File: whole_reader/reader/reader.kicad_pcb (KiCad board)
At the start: 2 copper layers, 50 x 58.5 mm, 61 parts, among them U1 LM386, U2 STM32F103C8T6, U3 MCP16301Hx-xCH, U4 MAX3232, Y1 16MHz

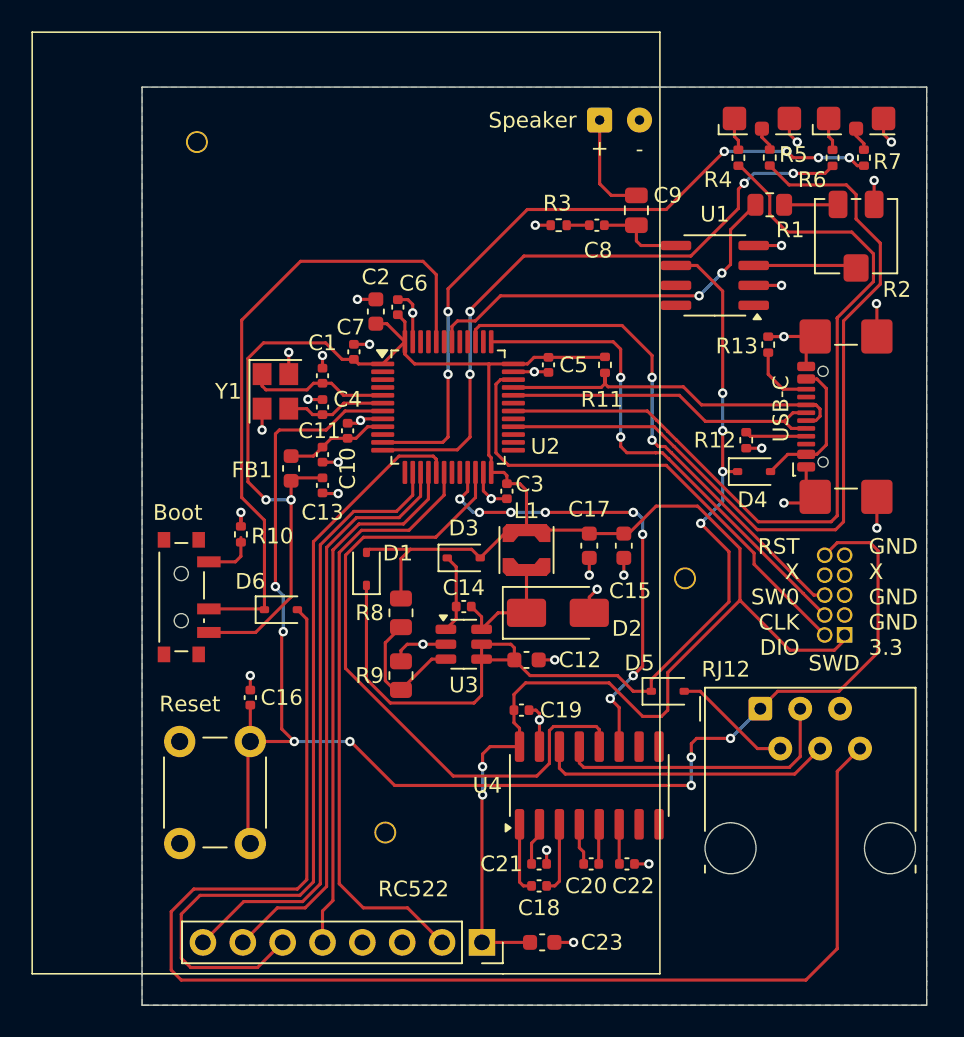
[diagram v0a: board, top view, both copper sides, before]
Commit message: Added toplayer ground copper pour
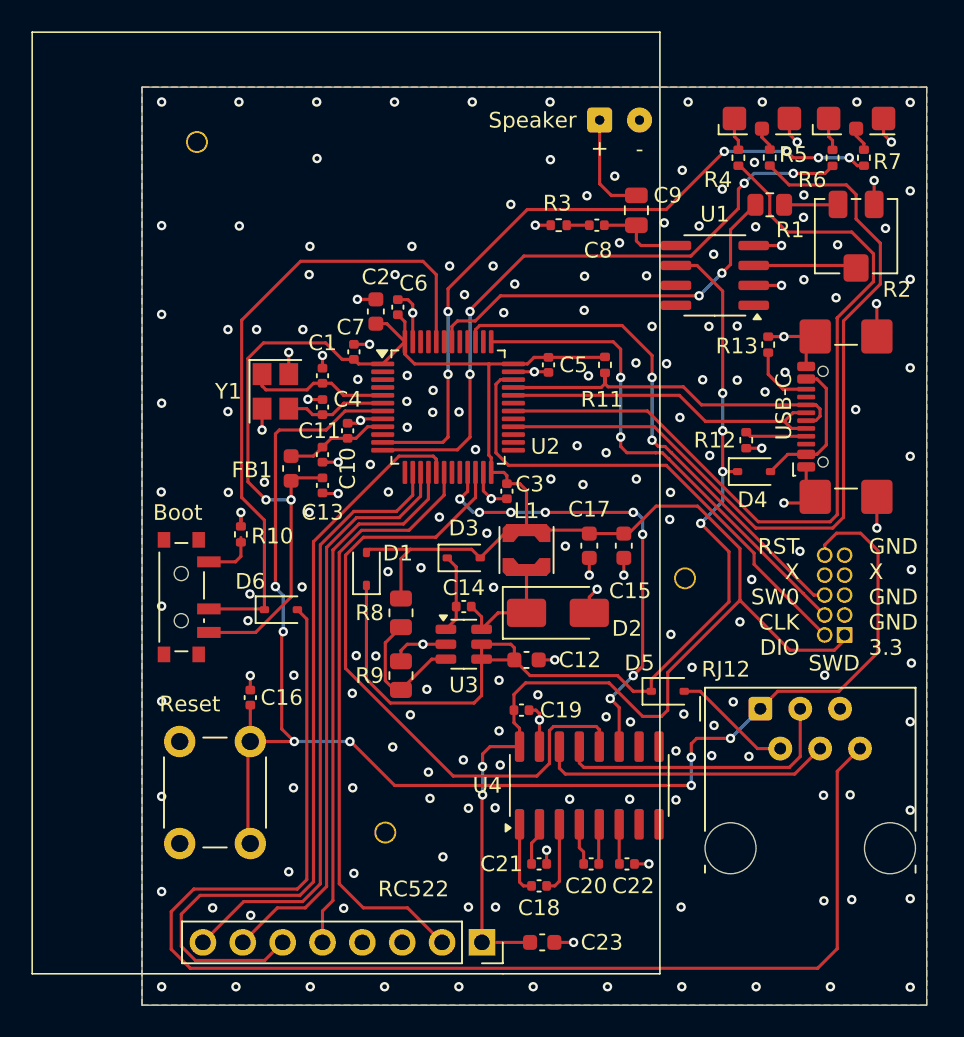
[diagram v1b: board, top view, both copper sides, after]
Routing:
- net Net-(D6-A): track 87.5 -> 86.1 mm
- net NRST: track 93.4 -> 94.3 mm
- net RFID_MOSI: track 52.1 -> 51.3 mm
- net GND: vias 34 -> 198
- added copper zone on F.Cu, net GND

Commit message: RST -> NRST, BOOT -> BOOT0, popis pre SWD
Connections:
- net BOOT renamed BOOT0
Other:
- board text added: "GND X GND GND 3.3V"
- board text added: "NRST X TRSW0 SWCLK SWDIO"
- board text removed: "GND X GND GND 3.3"
- board text removed: "RST X SW0 CLK DIO"
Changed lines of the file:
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@@
 	(net 19 "Net-(D5-A)")
 	(net 20 "Net-(D6-A)")
-	(net 21 "BOOT")
+	(net 21 "BOOT0")
 	(net 22 "SWCLK")
 	(net 23 "SWDIO")
@@
 			(size 0.7 1.5)
 			(layers "F.Cu" "F.Mask" "F.Paste")
-			(net 21 "BOOT")
+			(net 21 "BOOT0")
 			(pinfunction "B")
 			(pintype "passive")
@@
 			(layers "F.Cu" "F.Mask" "F.Paste")
 			(roundrect_rratio 0.25)
-			(net 21 "BOOT")
+			(net 21 "BOOT0")
 			(pinfunction "K")
 			(pintype "passive")
@@
 			(layers "F.Cu" "F.Mask" "F.Paste")
 			(roundrect_rratio 0.25)
-			(net 21 "BOOT")
+			(net 21 "BOOT0")
 			(pinfunction "BOOT0")
 			(pintype "input")
@@
 	(footprint "Connector_PinSocket_1.27mm:PinSocket_2x05_P1.27mm_Vertical"
 		(layer "B.Cu")
-		(at 177.27 62.41)
+		(at 177.2575 62.41)
 		(descr "Through hole straight socket strip, 2x05, 1.27mm pitch, double cols (from Kicad 4.0.7), script generated")
 		(tags "Through hole socket strip THT 2x05 1.27mm double row")
@@
 		)
 	)
-	(gr_text "RST\nX\nSW0\nCLK\nDIO"
-		(at 174.4 63.8 0)
+	(gr_text "NRST\nX\nTRSW0\nSWCLK\nSWDIO"
+		(at 174.625 63.675513 0)
 		(layer "F.SilkS")
 		(effects
@@
 		)
 	)
-	(gr_text "GND\nX\nGND\nGND\n3.3"
-		(at 178.8 63.8 0)
+	(gr_text "GND\nX\nGND\nGND\n3.3V"
+		(at 178.6 63.675513 0)
 		(layer "F.SilkS")
 		(effects
@@
 	)
 	(gr_text "SWD"
-		(at 176.6 64.8 0)
+		(at 176.6125 64.8 0)
 		(layer "F.SilkS")
 		(effects
@@
 	)
 	(via
-		(at 170.6 61.575)
+		(at 170.6 61.125)
 		(size 0.6)
 		(drill 0.3)

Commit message: Oprava pre PWR_FLAG, doplnenie dátumu a revízie
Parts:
- C16, C8: value 100nF -> 100 nF
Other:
- board text added: "UACS reader Rev. 1.0 (2025/04)"
- board text removed: "UACS reader HW ver. 1.0 (2025/04)"

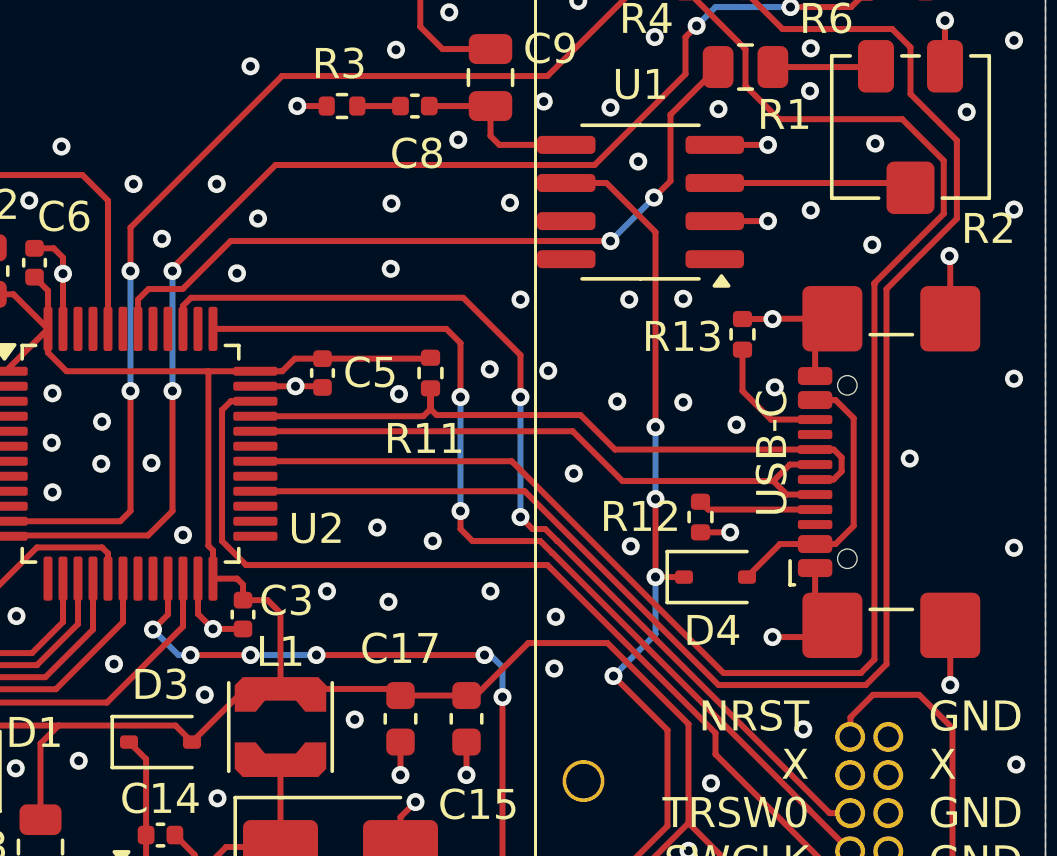
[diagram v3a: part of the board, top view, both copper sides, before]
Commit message: viring diferential pair
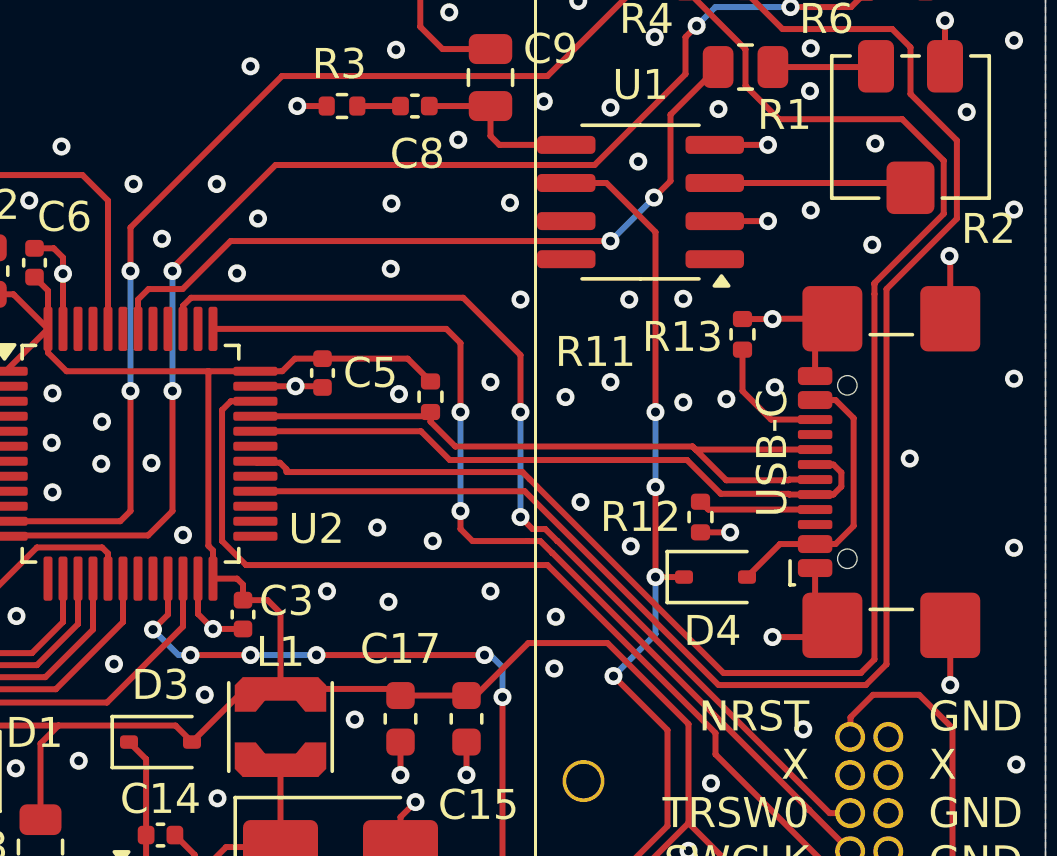
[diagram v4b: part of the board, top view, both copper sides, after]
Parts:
- moved R11 0.79 mm to (162.0, 46.0)
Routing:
- net USB_D+: track 22.9 -> 24.0 mm
- net USB_D-: track 21.2 -> 22.0 mm

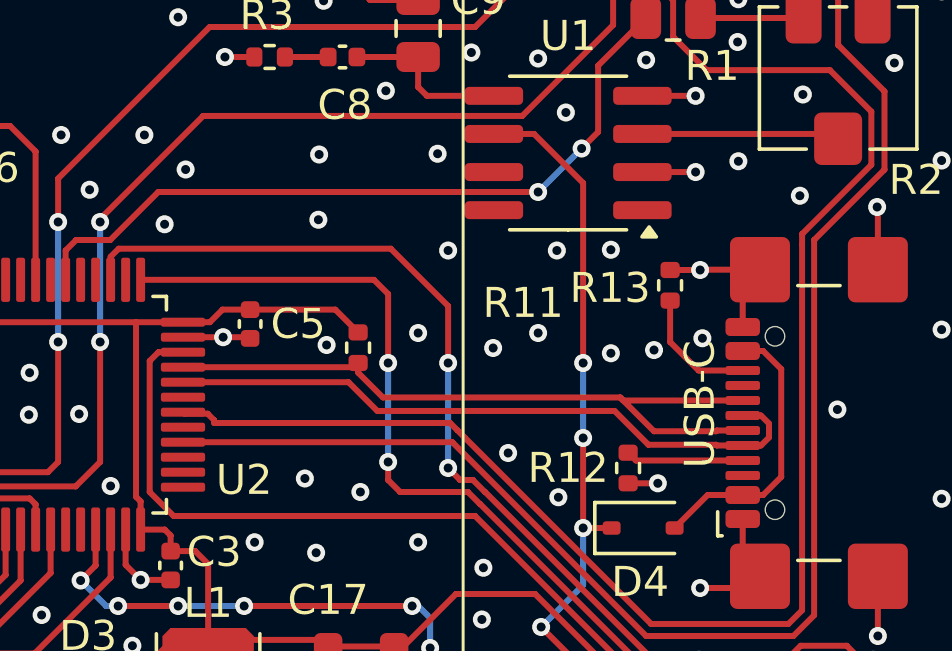
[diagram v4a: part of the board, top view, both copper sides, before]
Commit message: wired diferential pair on usb
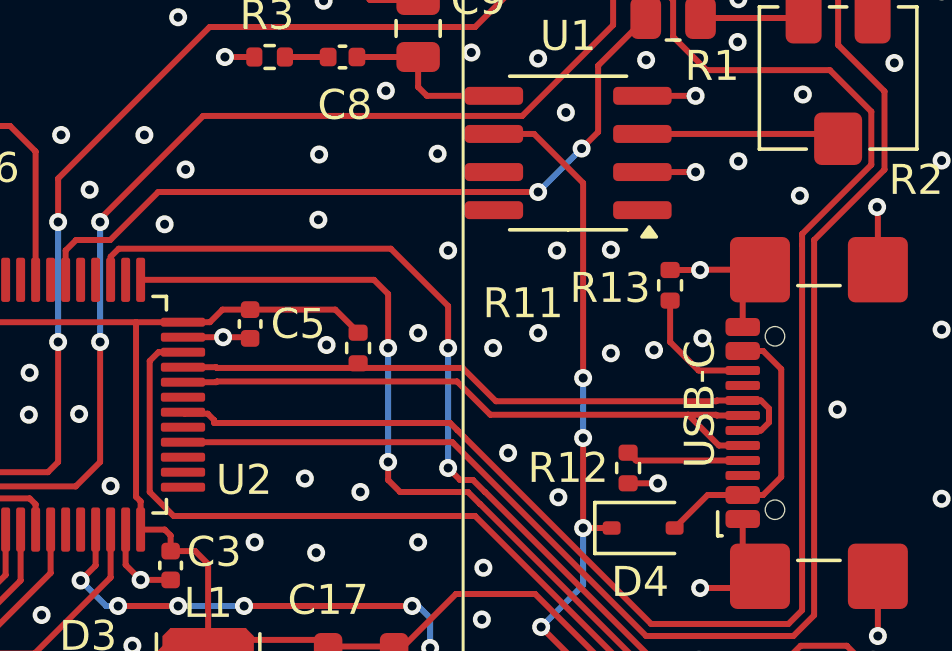
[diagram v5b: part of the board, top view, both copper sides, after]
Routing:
- net USB_D+: track 24.0 -> 21.6 mm
- net USB_D-: track 22.0 -> 21.4 mm
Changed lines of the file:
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@@
 	(footprint "Resistor_SMD:R_0402_1005Metric"
 		(layer "F.Cu")
-		(at 162 45.99 -90)
+		(at 162 46 -90)
 		(descr "Resistor SMD 0402 (1005 Metric), square (rectangular) end terminal, IPC_7351 nominal, (Body size source: IPC-SM-782 page 72, https://www.pcb-3d.com/wordpress/wp-content/uploads/ipc-sm-782a_amendment_1_and_2.pdf), generated with kicad-footprint-generator")
 		(tags "resistor")
@@
 	)
 	(segment
-		(start 169.5 46.5)
+		(start 169.5 47)
 		(end 169.5 40.5)
 		(width 0.2)
@@
 	)
 	(segment
+		(start 169.5 52)
+		(end 169.5 49)
+		(width 0.2)
+		(layer "F.Cu")
+		(net 8)
+	)
+	(segment
+		(start 167.865 38.865)
+		(end 166.525 38.865)
+		(width 0.2)
+		(layer "F.Cu")
+		(net 8)
+	)
+	(segment
 		(start 168.227094 55.172906)
 		(end 168.227094 55.427094)
@@
 	)
 	(segment
-		(start 167.865 38.865)
-		(end 166.525 38.865)
-		(width 0.2)
-		(layer "F.Cu")
-		(net 8)
-	)
-	(segment
 		(start 169.9 57.1)
 		(end 169.9 60.3)
@@
 	)
 	(segment
-		(start 156 63)
-		(end 154.138 63)
+		(start 169.5 40.5)
+		(end 167.865 38.865)
 		(width 0.2)
 		(layer "F.Cu")
@@
 	)
 	(segment
-		(start 169.5 52)
-		(end 169.5 49)
+		(start 156 63)
+		(end 154.138 63)
 		(width 0.2)
 		(layer "F.Cu")
@@
 	)
 	(segment
-		(start 169.5 40.5)
-		(end 167.865 38.865)
-		(width 0.2)
-		(layer "F.Cu")
-		(net 8)
-	)
-	(segment
 		(start 153.6546 66.7454)
 		(end 148.324 66.7454)
@@
 	)
 	(via
-		(at 169.5 46.5)
+		(at 169.5 47)
 		(size 0.6)
 		(drill 0.3)
@@
 	)
 	(segment
-		(start 169.5 52)
-		(end 169.5 53.9)
+		(start 169.5 49)
+		(end 169.5 47)
 		(width 0.2)
 		(layer "B.Cu")
@@
 	)
 	(segment
-		(start 169.5 49)
-		(end 169.5 46.5)
+		(start 169.5 52)
+		(end 169.5 53.9)
 		(width 0.2)
 		(layer "B.Cu")
@@
 	)
 	(segment
+		(start 163 46)
+		(end 163 44.2)
+		(width 0.2)
+		(layer "F.Cu")
+		(net 22)
+	)
+	(segment
 		(start 165.2329 50.8)
 		(end 165.2339 50.801)
@@
 	)
 	(segment
-		(start 163 46.5)
-		(end 163 44.2)
-		(width 0.2)
-		(layer "F.Cu")
-		(net 22)
-	)
-	(segment
 		(start 163 44.2)
 		(end 162.5275 43.7275)
@@
 	)
 	(via
-		(at 163 46.5)
+		(at 163 46)
 		(size 0.6)
 		(drill 0.3)
@@
 	)
 	(segment
-		(start 163 46.5)
+		(start 163 46)
 		(end 163 49.8)
 		(width 0.2)
@@
 	)
 	(segment
-		(start 165 46.5)
+		(start 165 46)
 		(end 165 44.6)
 		(width 0.2)
@@
 	)
 	(segment
-		(start 153.75 42.9576)
-		(end 153.75 43.7275)
+		(start 165 44.6)
+		(end 163.09 42.69)
 		(width 0.2)
 		(layer "F.Cu")
@@
 	)
 	(segment
-		(start 165 44.6)
-		(end 163.09 42.69)
+		(start 153.75 42.9576)
+		(end 153.75 43.7275)
 		(width 0.2)
 		(layer "F.Cu")
@@
 	)
 	(via
-		(at 165 46.5)
+		(at 165 46)
 		(size 0.6)
 		(drill 0.3)
@@
 	(segment
 		(start 165 50)
-		(end 165 46.5)
+		(end 165 46)
 		(width 0.2)
 		(layer "B.Cu")
@@
 	)
 	(segment
-		(start 173.957499 48.75)
-		(end 173.932499 48.775)
-		(width 0.2)
-		(layer "F.Cu")
-		(net 25)
-	)
-	(segment
-		(start 171.861708 48.775)
-		(end 170.735728 47.64902)
+		(start 156.1625 46.64)
+		(end 157.268751 46.64)
 		(width 0.2)
 		(layer "F.Cu")
@@
 	)
 	(segment
-		(start 161.86 46.64)
-		(end 156.1625 46.64)
+		(start 175.428824 47.75)
+		(end 174.82 47.75)
 		(width 0.2)
 		(layer "F.Cu")
@@
 	)
 	(segment
-		(start 170.836708 47.75)
-		(end 170.735728 47.64902)
+		(start 175.428824 48.75)
+		(end 175.696 48.482824)
 		(width 0.2)
 		(layer "F.Cu")
@@
 	)
 	(segment
-		(start 174.82 47.75)
-		(end 170.836708 47.75)
+		(start 157.268751 46.64)
+		(end 157.293751 46.665)
 		(width 0.2)
 		(layer "F.Cu")
@@
 	(segment
 		(start 174.82 48.75)
-		(end 173.957499 48.75)
+		(end 175.428824 48.75)
 		(width 0.2)
 		(layer "F.Cu")
@@
 	)
 	(segment
-		(start 162.827219 47.64902)
-		(end 162 46.821801)
+		(start 173.957499 47.75)
+		(end 174.82 47.75)
 		(width 0.2)
 		(layer "F.Cu")
@@
 	)
 	(segment
-		(start 162 46.821801)
-		(end 162 46.5)
+		(start 175.696 48.482824)
+		(end 175.696 48.017176)
 		(width 0.2)
 		(layer "F.Cu")
@@
 	)
 	(segment
-		(start 162 46.5)
-		(end 161.86 46.64)
+		(start 166.593198 47.775)
+		(end 173.932499 47.775)
 		(width 0.2)
 		(layer "F.Cu")
@@
 	)
 	(segment
-		(start 173.932499 48.775)
-		(end 171.861708 48.775)
+		(start 157.293751 46.665)
+		(end 165.483198 46.665)
 		(width 0.2)
 		(layer "F.Cu")
@@
 	)
 	(segment
-		(start 170.735728 47.64902)
-		(end 162.827219 47.64902)
+		(start 175.696 48.017176)
+		(end 175.428824 47.75)
 		(width 0.2)
 		(layer "F.Cu")
@@
 	)
 	(segment
-		(start 174.82 49.25)
-		(end 173.957499 49.25)
+		(start 165.483198 46.665)
+		(end 166.593198 47.775)
 		(width 0.2)
 		(layer "F.Cu")
-		(net 26)
+		(net 25)
 	)
 	(segment
-		(start 173.957499 49.25)
-		(end 173.932499 49.225)
+		(start 173.932499 47.775)
+		(end 173.957499 47.75)
 		(width 0.2)
 		(layer "F.Cu")
-		(net 26)
+		(net 25)
 	)
 	(segment
-		(start 162.640801 48.099)
-		(end 161.681801 47.14)
+		(start 156.1625 47.14)
+		(end 157.268751 47.14)
 		(width 0.2)
 		(layer "F.Cu")
@@
 	)
 	(segment
-		(start 173.932499 49.225)
-		(end 171.67534 49.225)
+		(start 174.82 49.25)
+		(end 174.025 49.25)
 		(width 0.2)
 		(layer "F.Cu")
@@
 	)
 	(segment
-		(start 175.428824 49.25)
-		(end 174.82 49.25)
+		(start 174.025 49.25)
+		(end 173 48.225)
 		(width 0.2)
 		(layer "F.Cu")
@@
 	)
 	(segment
-		(start 175.696 48.982824)
-		(end 175.428824 49.25)
+		(start 166.406802 48.225)
+		(end 173 48.225)
 		(width 0.2)
 		(layer "F.Cu")
@@
 	)
 	(segment
-		(start 175.428824 48.25)
-		(end 175.696 48.517176)
+		(start 173 48.225)
+		(end 173.932499 48.225)
 		(width 0.2)
 		(layer "F.Cu")
@@
 	)
 	(segment
-		(start 175.696 48.517176)
-		(end 175.696 48.982824)
+		(start 173.932499 48.225)
+		(end 173.957499 48.25)
 		(width 0.2)
 		(layer "F.Cu")
@@
 	)
 	(segment
-		(start 161.681801 47.14)
-		(end 156.1625 47.14)
+		(start 165.296802 47.115)
+		(end 166.406802 48.225)
 		(width 0.2)
 		(layer "F.Cu")
@@
 	)
 	(segment
-		(start 170.54934 48.099)
-		(end 162.640801 48.099)
+		(start 157.268751 47.14)
+		(end 157.293751 47.115)
 		(width 0.2)
 		(layer "F.Cu")
@@
 	)
 	(segment
-		(start 171.67534 49.225)
-		(end 170.54934 48.099)
+		(start 157.293751 47.115)
+		(end 165.296802 47.115)
 		(width 0.2)
 		(layer "F.Cu")
@@
 	)
 	(segment
-		(start 174.82 48.25)
-		(end 175.428824 48.25)
+		(start 173.957499 48.25)
+		(end 174.82 48.25)
 		(width 0.2)
 		(layer "F.Cu")

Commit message: Pridanie testovacích bodov
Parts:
- added TP1: +3.3 V, TestPoint:TestPoint_THTPad_D1.0mm_Drill0.5mm, F.Cu at (159.2, 53.0)
- added TP2: V+, TestPoint:TestPoint_THTPad_D1.0mm_Drill0.5mm, F.Cu at (167.4, 55.4)
- added TP3: Audio, TestPoint:TestPoint_THTPad_D1.0mm_Drill0.5mm, F.Cu at (162.8, 40.8)
- added TP4: GND, TestPoint:TestPoint_THTPad_D1.0mm_Drill0.5mm, F.Cu at (164.2, 53.0)
- C1, C4: value 10pF -> 10 pF
- C10: value 10nF -> 10 nF
- C11, C13: value 1µF -> 1 µF
- C2, C23: value 10µF -> 10 µF
- C9: value 100µF -> 100 µF
- FB1: value 120R -> 120 R
- R1: value 100K -> 100 K
- R10: value 10k -> 10 K
- R11: value 1k5 -> 1500 R
- R12, R13: value 5K1 -> 5100 R
- R2: value 10K -> 10 K
- R3: value 10R -> 10 R
- R4, R5, R6, R7: value 330R -> 330 R
- R8: value 75 k -> 75 K
- R9: value 24k -> 24 K
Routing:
- net +3.3V: track 150.1 -> 152.8 mm
- net V+: track 65.7 -> 66.0 mm, vias 4 -> 3
- net GND: vias 198 -> 200
